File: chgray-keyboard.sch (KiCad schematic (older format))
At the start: 1 part, among them U1 Teensy2.0_(C)

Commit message: laying out the keys with logan
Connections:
- wire segments 69 -> 72
- no-connect marks 12 -> 11
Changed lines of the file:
@@
 $EndDescr
 $Sheet
-S 7300 1800 2100 1850
+S 7300 1800 2000 2800
 U 589645BF
 F0 "Keyboard Keys" 60
 F1 "Keys.sch" 60
 F2 "KEY_COL0" I L 7300 2000 60
-F3 "KEY_ROW0" I R 9400 1950 60
-F4 "KEY_ROW1" I R 9400 2150 60
+F3 "KEY_ROW0" I R 9300 1950 60
+F4 "KEY_ROW1" I R 9300 2150 60
 F5 "KEY_COL1" I L 7300 2150 60
-F6 "KEY_ROW2" I R 9400 2350 50
-F7 "KEY_ROW3" I R 9400 2550 50
-F8 "KEY_ROW4" I R 9400 2750 50
-F9 "KEY_ROW5" I R 9400 2900 50
+F6 "KEY_ROW2" I R 9300 2350 50
+F7 "KEY_ROW3" I R 9300 2550 50
+F8 "KEY_ROW4" I R 9300 2750 50
+F9 "KEY_ROW5" I R 9300 2900 50
 F10 "KEY_COL2" I L 7300 2300 50
 F11 "KEY_COL3" I L 7300 2450 50
@@
 F17 "KEY_COL9" I L 7300 3350 50
 F18 "KEY_COL10" I L 7300 3500 50
+F19 "KEY_COL11" I L 7300 3700 50
 $EndSheet
 Wire Wire Line
@@
 NoConn ~ 4550 6350
 NoConn ~ 4550 6450
-NoConn ~ 4550 6550
 NoConn ~ 2150 6250
 NoConn ~ 2150 6350
@@
 	2000 7150 2000 7650
 Connection ~ 2000 7150
+Wire Wire Line
+	7300 3700 4750 3700
+Wire Wire Line
+	4750 3700 4750 6550
+Wire Wire Line
+	4750 6550 4550 6550
 $EndSCHEMATC

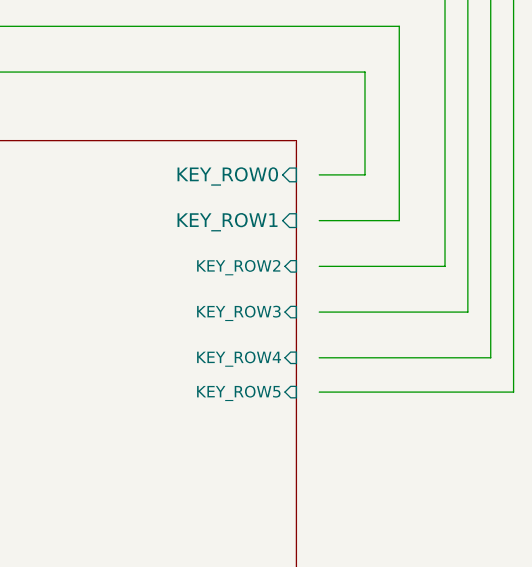
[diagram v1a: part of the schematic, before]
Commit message: add 1.75U switch
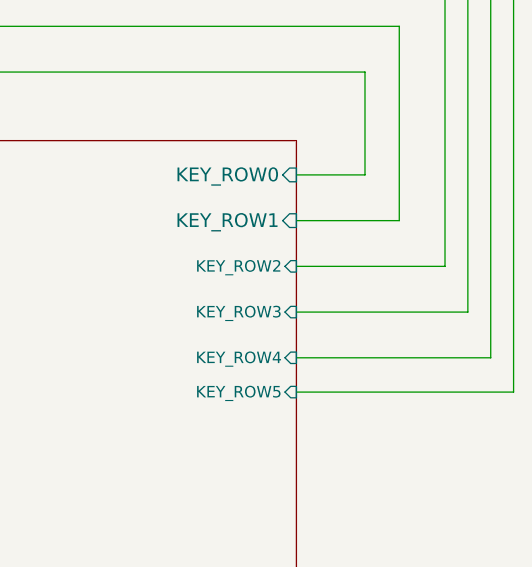
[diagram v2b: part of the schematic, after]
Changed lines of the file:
@@
 	7300 2000 1650 2000
 Wire Wire Line
-	9750 2150 9400 2150
-Wire Wire Line
-	9400 1950 9600 1950
-Wire Wire Line
 	1500 2150 7300 2150
-Wire Wire Line
-	9400 2350 9950 2350
 Wire Wire Line
 	9950 2350 9950 1000
 Wire Wire Line
 	9950 1000 1000 1000
-Wire Wire Line
-	9400 2550 10050 2550
 Wire Wire Line
 	10050 2550 10050 850
@@
 	10150 700  10150 2750
 Wire Wire Line
-	10150 2750 9400 2750
-Wire Wire Line
 	10250 2900 10250 550
 Wire Wire Line
 	10250 550  700  550
-Wire Wire Line
-	10250 2900 9400 2900
 Wire Wire Line
 	2250 5850 2150 5850
@@
 Wire Wire Line
 	4750 6550 4550 6550
+Wire Wire Line
+	9300 1950 9600 1950
+Wire Wire Line
+	9300 2150 9750 2150
+Wire Wire Line
+	9300 2350 9950 2350
+Wire Wire Line
+	9300 2550 10050 2550
+Wire Wire Line
+	9300 2750 10150 2750
+Wire Wire Line
+	9300 2900 10250 2900
 $EndSCHEMATC

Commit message: working on rgb
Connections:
- wire segments 72 -> 87
- no-connect marks 11 -> 7
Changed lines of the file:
@@
 $Descr A 11000 8500
 encoding utf-8
-Sheet 1 2
+Sheet 1 3
 Title ""
 Date ""
@@
 F18 "KEY_COL10" I L 7300 3500 50
 F19 "KEY_COL11" I L 7300 3700 50
+F20 "KEY_COL12" I L 7300 3950 50
+F21 "KEY_COL13" I L 7300 4150 50
 $EndSheet
 Wire Wire Line
@@
 Wire Wire Line
 	1500 2150 7300 2150
-Wire Wire Line
-	9950 2350 9950 1000
-Wire Wire Line
-	9950 1000 1000 1000
 Wire Wire Line
 	10050 2550 10050 850
@@
 	900  850  900  7250
 Wire Wire Line
-	1000 1000 1000 7050
-Wire Wire Line
 	1150 6950 2150 6950
 Wire Wire Line
@@
 NoConn ~ 4550 5950
 NoConn ~ 4550 6050
-NoConn ~ 4550 6150
-NoConn ~ 4550 6250
-NoConn ~ 4550 6350
-NoConn ~ 4550 6450
 NoConn ~ 2150 6250
 NoConn ~ 2150 6350
@@
 	9300 2150 9750 2150
 Wire Wire Line
-	9300 2350 9950 2350
-Wire Wire Line
 	9300 2550 10050 2550
 Wire Wire Line
@@
 Wire Wire Line
 	9300 2900 10250 2900
+$Sheet
+S 8250 5700 1600 600
+U 6096EA02
+F0 "Sheet6096EA01" 50
+F1 "RGB-Circuit.sch" 50
+F2 "LED_INPUT" I L 8250 5850 50
+F3 "LED_VDD" I L 8250 6150 50
+$EndSheet
+Wire Wire Line
+	8250 5850 6300 5850
+Wire Wire Line
+	6300 5850 6300 6450
+Wire Wire Line
+	6300 6450 4550 6450
+Wire Wire Line
+	8250 6150 6400 6150
+Wire Wire Line
+	6400 6150 6400 7450
+Wire Wire Line
+	6400 7450 1650 7450
+Wire Wire Line
+	1650 7450 1650 7050
+Wire Wire Line
+	1650 7050 2150 7050
+Wire Wire Line
+	9300 2350 9450 2350
+Wire Wire Line
+	9450 2350 9450 5550
+Wire Wire Line
+	9450 5550 4900 5550
+Wire Wire Line
+	4900 5550 4900 6150
+Wire Wire Line
+	4900 6150 4550 6150
+Wire Wire Line
+	4550 6250 6800 6250
+Wire Wire Line
+	6800 6250 6800 3950
+Wire Wire Line
+	6800 3950 7300 3950
+Wire Wire Line
+	7300 4150 7000 4150
+Wire Wire Line
+	7000 4150 7000 6350
+Wire Wire Line
+	7000 6350 4550 6350
 $EndSCHEMATC

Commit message: rgb
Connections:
- wire segments 87 -> 90
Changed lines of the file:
@@
 	2000 7150 2150 7150
 $Comp
-L power:GND #PWR0101
+L power:GND #PWR01
 U 1 1 6093A5EC
 P 2000 7650
-F 0 "#PWR0101" H 2000 7400 50  0001 C CNN
+F 0 "#PWR01" H 2000 7400 50  0001 C CNN
 F 1 "GND" H 2005 7477 50  0000 C CNN
 F 2 "" H 2000 7650 50  0001 C CNN
@@
 Wire Wire Line
 	9300 2900 10250 2900
-$Sheet
-S 8250 5700 1600 600
-U 6096EA02
-F0 "Sheet6096EA01" 50
-F1 "RGB-Circuit.sch" 50
-F2 "LED_INPUT" I L 8250 5850 50
-F3 "LED_VDD" I L 8250 6150 50
-$EndSheet
 Wire Wire Line
 	8250 5850 6300 5850
@@
 Wire Wire Line
 	7000 6350 4550 6350
+$Sheet
+S 8250 5700 1600 600
+U 6096EA02
+F0 "Sheet6096EA01" 50
+F1 "RGB-Circuit.sch" 50
+F2 "5V" I L 8250 6150 50
+F3 "VDD" I L 8250 6000 50
+F4 "INPUT" I L 8250 5850 50
+$EndSheet
+$Comp
+L power:GND #PWR02
+U 1 1 60D5C704
+P 7950 6550
+F 0 "#PWR02" H 7950 6300 50  0001 C CNN
+F 1 "GND" H 7955 6377 50  0000 C CNN
+F 2 "" H 7950 6550 50  0001 C CNN
+F 3 "" H 7950 6550 50  0001 C CNN
+	1    7950 6550
+	1    0    0    -1
+$EndComp
+Wire Wire Line
+	7950 6550 7900 6550
+Wire Wire Line
+	7900 6550 7900 6000
+Wire Wire Line
+	7900 6000 8250 6000
 $EndSCHEMATC

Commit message: keyboard
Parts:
- added J1: Conn_01x01_Female, Connector_PinHeader_1.27mm:PinHeader_2x07_P1.27mm_Vertical, symbol Connector_Generic:Conn_02x07_Odd_Even
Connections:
- wire segments 90 -> 108
- no-connect marks 7 -> 11
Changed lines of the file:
@@
 Wire Wire Line
 	1500 2150 1500 6750
-Wire Wire Line
-	1650 6650 2150 6650
-Wire Wire Line
-	1650 2000 1650 6650
 NoConn ~ 4550 5850
 NoConn ~ 4550 5950
-NoConn ~ 4550 6050
 NoConn ~ 2150 6250
 NoConn ~ 2150 6350
-NoConn ~ 2150 6450
-NoConn ~ 2150 6550
 Wire Wire Line
 	2150 5950 800  5950
@@
 $EndComp
 Wire Wire Line
-	2000 7150 2000 7650
+	2000 7150 2000 7600
 Connection ~ 2000 7150
 Wire Wire Line
@@
 	9300 2900 10250 2900
 Wire Wire Line
-	8250 5850 6300 5850
-Wire Wire Line
-	6300 5850 6300 6450
-Wire Wire Line
-	6300 6450 4550 6450
-Wire Wire Line
-	8250 6150 6400 6150
-Wire Wire Line
-	6400 6150 6400 7450
-Wire Wire Line
-	6400 7450 1650 7450
-Wire Wire Line
-	1650 7450 1650 7050
-Wire Wire Line
-	1650 7050 2150 7050
-Wire Wire Line
 	9300 2350 9450 2350
 Wire Wire Line
@@
 Wire Wire Line
 	4550 6250 6800 6250
-Wire Wire Line
-	6800 6250 6800 3950
 Wire Wire Line
 	6800 3950 7300 3950
@@
 $EndSheet
 $Comp
-L power:GND #PWR02
-U 1 1 60D5C704
-P 7950 6550
-F 0 "#PWR02" H 7950 6300 50  0001 C CNN
-F 1 "GND" H 7955 6377 50  0000 C CNN
-F 2 "" H 7950 6550 50  0001 C CNN
-F 3 "" H 7950 6550 50  0001 C CNN
-	1    7950 6550
+L Connector_Generic:Conn_02x07_Odd_Even J1
+U 1 1 609EE309
+P 7300 6900
+F 0 "J1" H 7350 7417 50  0000 C CNN
+F 1 "Conn_01x01_Female" H 7350 7326 50  0000 C CNN
+F 2 "Connector_PinHeader_1.27mm:PinHeader_2x07_P1.27mm_Vertical" H 7300 6900 50  0001 C CNN
+F 3 "~" H 7300 6900 50  0001 C CNN
+	1    7300 6900
 	1    0    0    -1
 $EndComp
 Wire Wire Line
-	7950 6550 7900 6550
+	7100 6600 6600 6600
 Wire Wire Line
-	7900 6550 7900 6000
+	6600 6600 6600 7600
 Wire Wire Line
-	7900 6000 8250 6000
+	6600 7600 2000 7600
+Connection ~ 2000 7600
+Wire Wire Line
+	2000 7600 2000 7650
+Wire Wire Line
+	6800 6250 6800 3950
+Wire Wire Line
+	6700 6050 6700 7200
+Wire Wire Line
+	6700 7200 7100 7200
+Wire Wire Line
+	7600 7200 8100 7200
+Wire Wire Line
+	8100 7200 8100 6150
+Wire Wire Line
+	8100 6150 8250 6150
+Wire Wire Line
+	7600 6600 7950 6600
+Wire Wire Line
+	7950 6600 7950 6000
+Wire Wire Line
+	7950 6000 8250 6000
+Wire Wire Line
+	7600 6700 8050 6700
+Wire Wire Line
+	8050 6700 8050 5850
+Wire Wire Line
+	8050 5850 8250 5850
+Wire Wire Line
+	4550 6450 7000 6450
+Wire Wire Line
+	7000 6450 7000 6700
+Wire Wire Line
+	7000 6700 7100 6700
+Wire Wire Line
+	4550 6050 6700 6050
+Wire Wire Line
+	2150 6450 1650 6450
+Wire Wire Line
+	1650 6450 1650 2000
+Wire Wire Line
+	7100 6800 6500 6800
+Wire Wire Line
+	6500 6800 6500 7950
+Wire Wire Line
+	6500 7950 1750 7950
+Wire Wire Line
+	1750 7950 1750 6550
+Wire Wire Line
+	1750 6550 2150 6550
+Wire Wire Line
+	2150 6650 1850 6650
+Wire Wire Line
+	1850 6650 1850 7850
+Wire Wire Line
+	1850 7850 6650 7850
+Wire Wire Line
+	6650 7850 6650 6900
+Wire Wire Line
+	6650 6900 7100 6900
+NoConn ~ 2150 7050
+NoConn ~ 7100 7000
+NoConn ~ 7100 7100
+NoConn ~ 7600 7000
+NoConn ~ 7600 7100
+NoConn ~ 7600 6900
+NoConn ~ 7600 6800
 $EndSCHEMATC

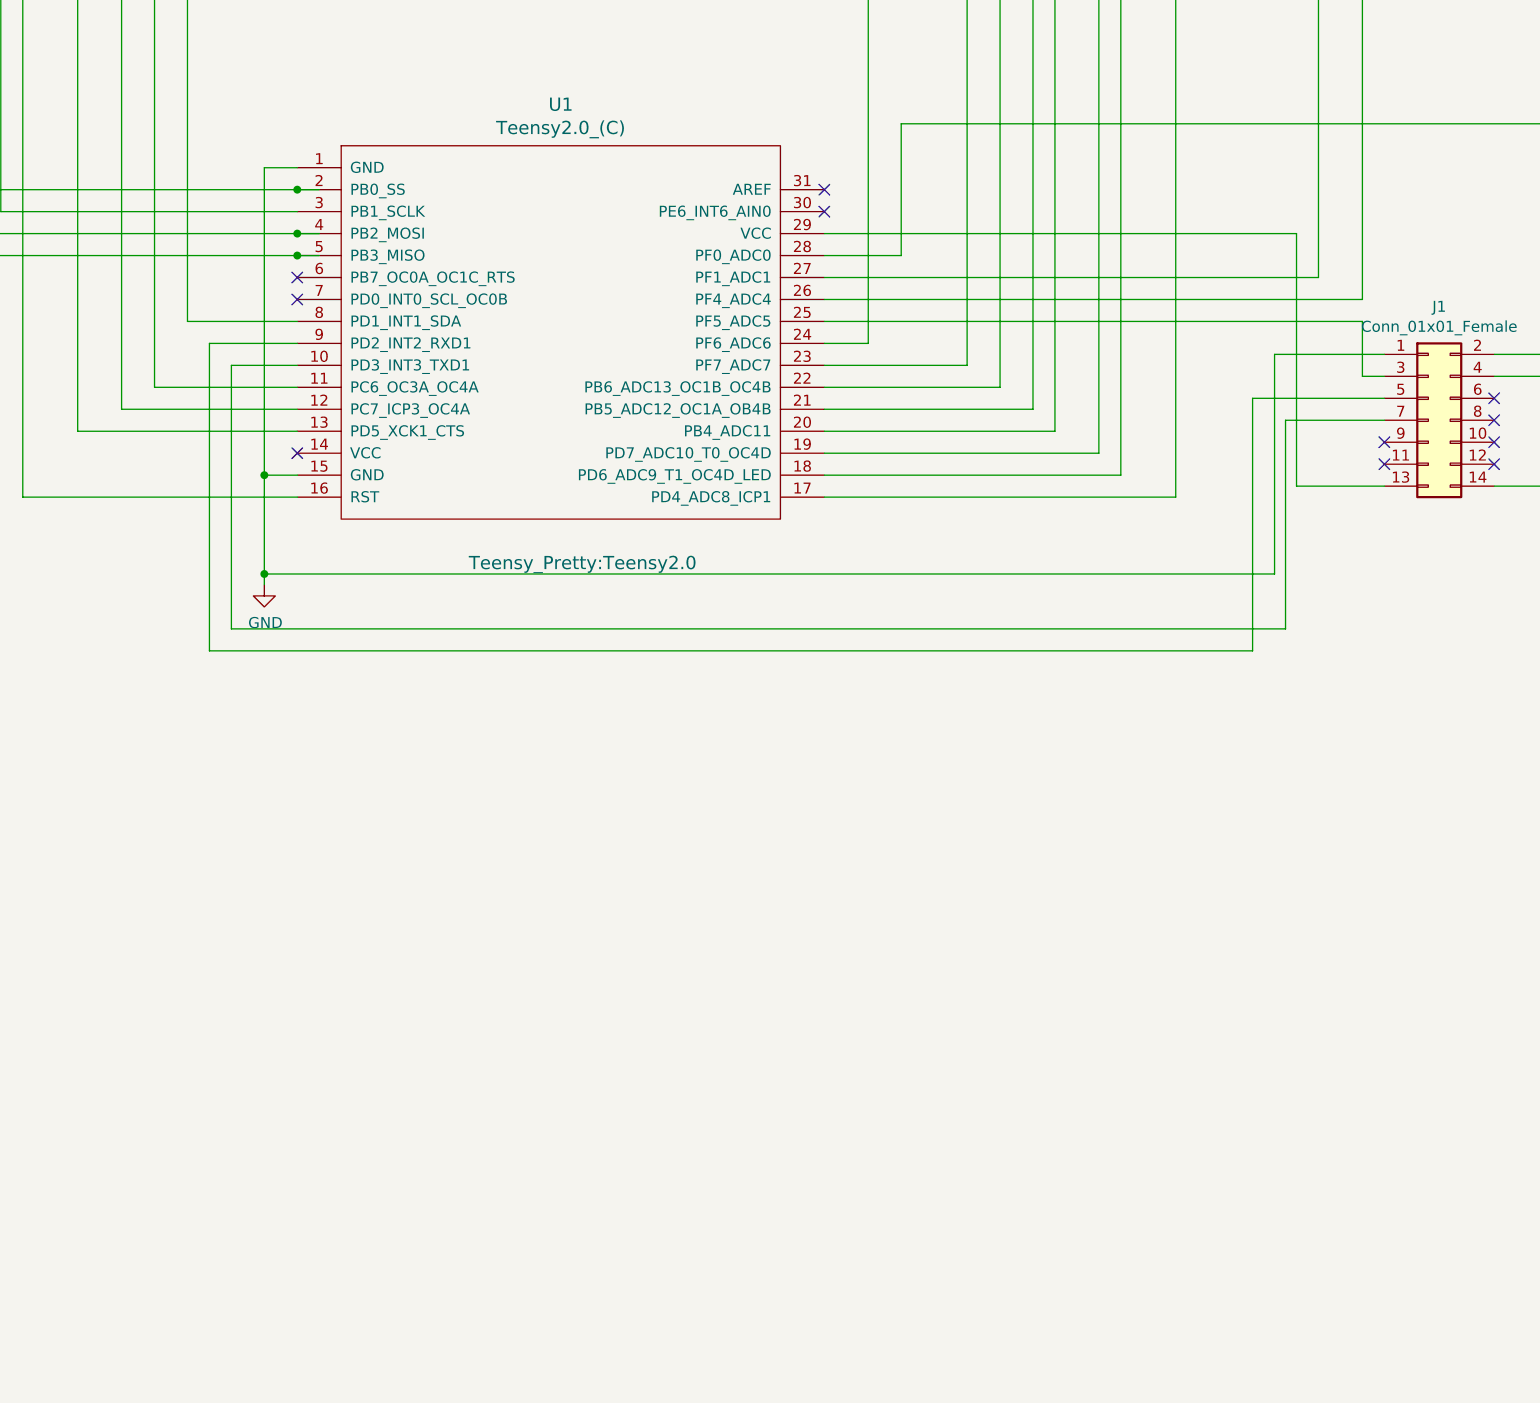
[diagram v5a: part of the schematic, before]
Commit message: Logan signed off on board location
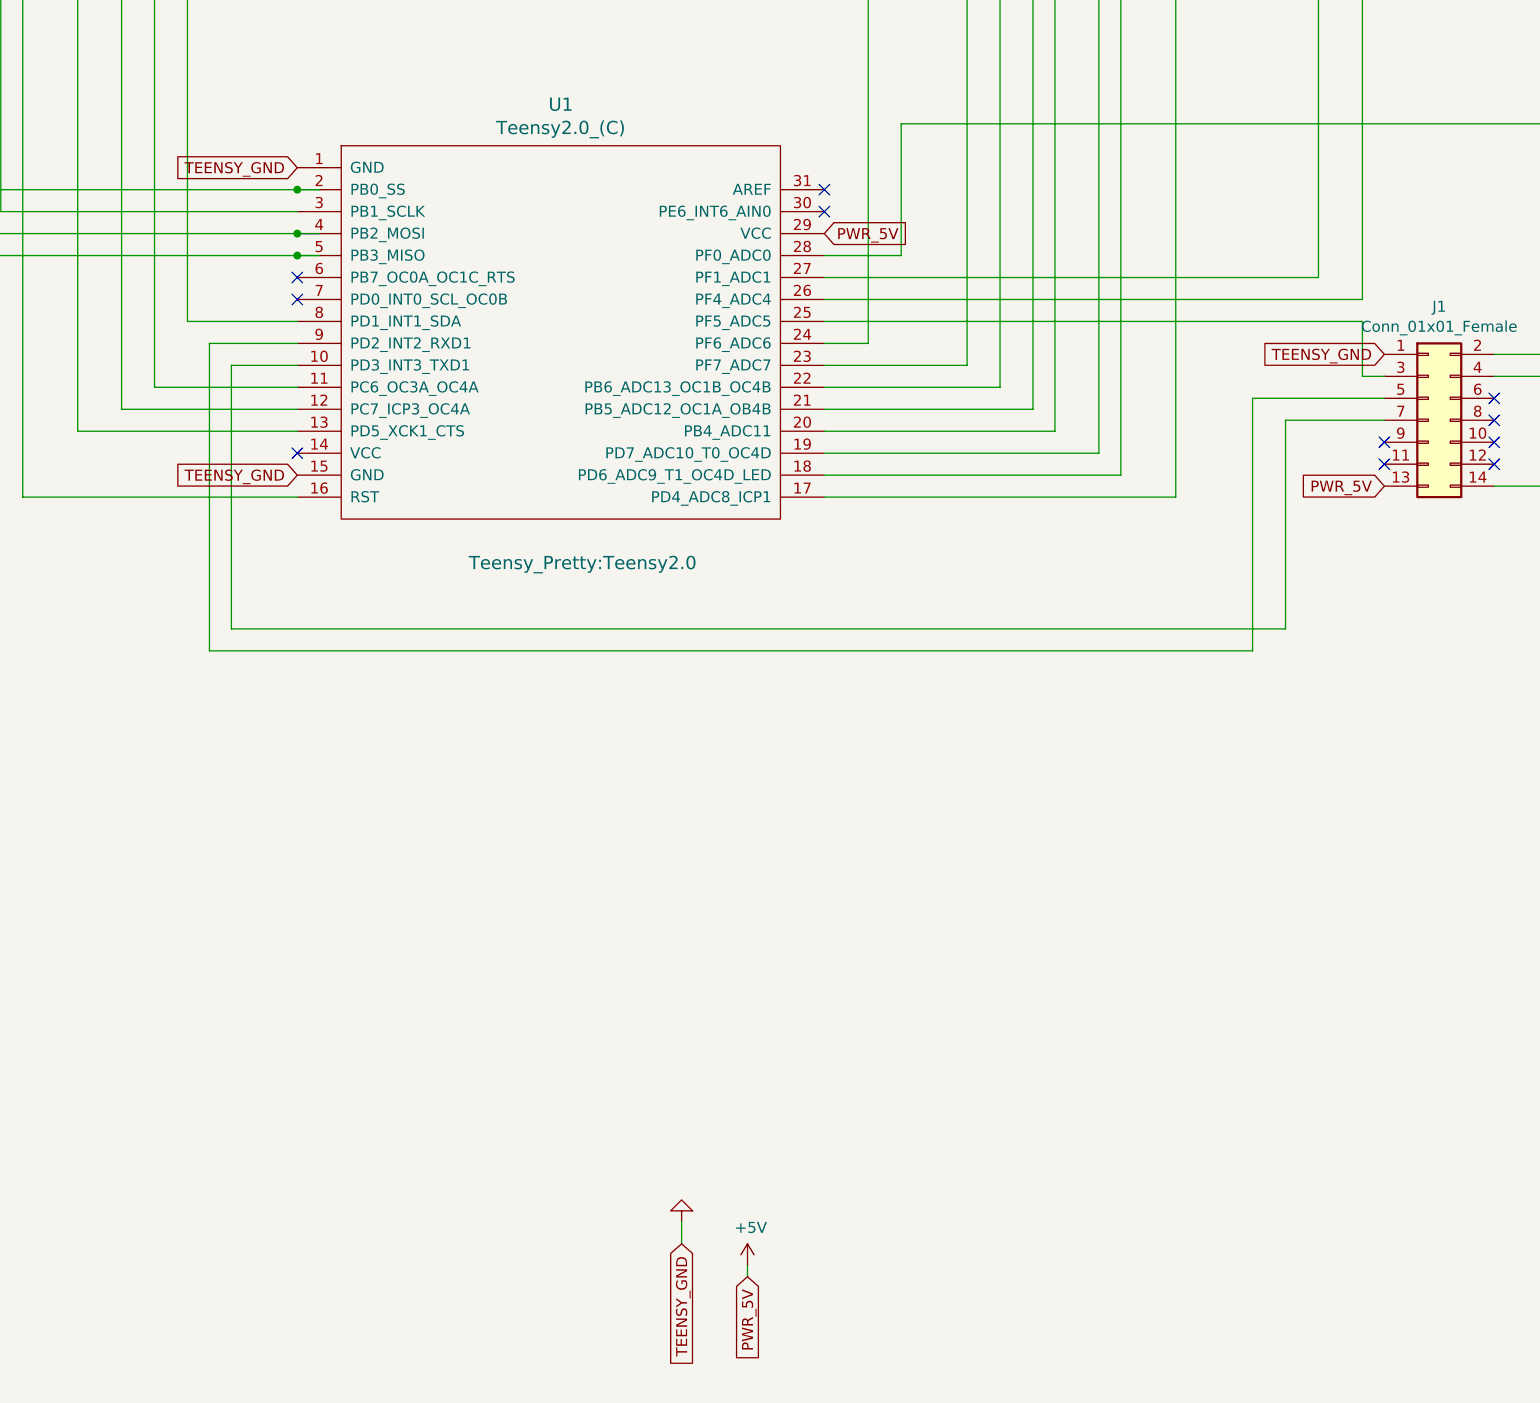
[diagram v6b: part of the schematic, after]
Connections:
- net labels added: +5V, PWR_5V, TEENSY_GND
- wire segments 108 -> 99
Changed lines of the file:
@@
 	800  5950 800  700
-Wire Wire Line
-	2150 5750 2000 5750
-Wire Wire Line
-	2000 5750 2000 7150
-Wire Wire Line
-	2000 7150 2150 7150
-$Comp
-L power:GND #PWR01
-U 1 1 6093A5EC
-P 2000 7650
-F 0 "#PWR01" H 2000 7400 50  0001 C CNN
-F 1 "GND" H 2005 7477 50  0000 C CNN
-F 2 "" H 2000 7650 50  0001 C CNN
-F 3 "" H 2000 7650 50  0001 C CNN
-	1    2000 7650
-	1    0    0    -1
-$EndComp
-Wire Wire Line
-	2000 7150 2000 7600
-Connection ~ 2000 7150
 Wire Wire Line
 	7300 3700 4750 3700
@@
 $EndComp
 Wire Wire Line
-	7100 6600 6600 6600
-Wire Wire Line
-	6600 6600 6600 7600
-Wire Wire Line
-	6600 7600 2000 7600
-Connection ~ 2000 7600
-Wire Wire Line
-	2000 7600 2000 7650
-Wire Wire Line
 	6800 6250 6800 3950
-Wire Wire Line
-	6700 6050 6700 7200
-Wire Wire Line
-	6700 7200 7100 7200
-Wire Wire Line
-	7600 7200 8100 7200
 Wire Wire Line
 	8100 7200 8100 6150
 Wire Wire Line
 	8100 6150 8250 6150
-Wire Wire Line
-	7600 6600 7950 6600
 Wire Wire Line
 	7950 6600 7950 6000
@@
 Wire Wire Line
 	7000 6700 7100 6700
-Wire Wire Line
-	4550 6050 6700 6050
 Wire Wire Line
 	2150 6450 1650 6450
@@
 NoConn ~ 7600 6900
 NoConn ~ 7600 6800
+Wire Wire Line
+	7600 7200 8100 7200
+$Comp
+L power:+5V #PWR0101
+U 1 1 6123E4B4
+P 4200 10750
+F 0 "#PWR0101" H 4200 10600 50  0001 C CNN
+F 1 "+5V" H 4215 10923 50  0000 C CNN
+F 2 "" H 4200 10750 50  0001 C CNN
+F 3 "" H 4200 10750 50  0001 C CNN
+	1    4200 10750
+	1    0    0    -1
+$EndComp
+Text GLabel 7100 7200 0    50   Input ~ 0
+PWR_5V
+Text GLabel 4200 10800 3    50   Input ~ 0
+PWR_5V
+Text GLabel 4550 6050 2    50   Input ~ 0
+PWR_5V
+Text GLabel 3900 10650 3    50   Input ~ 0
+TEENSY_GND
+Text GLabel 7100 6600 0    50   Input ~ 0
+TEENSY_GND
+Text GLabel 2150 5750 0    50   Input ~ 0
+TEENSY_GND
+Text GLabel 2150 7150 0    50   Input ~ 0
+TEENSY_GND
+$Comp
+L Cherry-Symbol:GND #PWR0102
+U 1 1 61266E57
+P 3900 10500
+F 0 "#PWR0102" H 3900 10500 30  0001 C CNN
+F 1 "GND" H 3900 10430 30  0001 C CNN
+F 2 "" H 3900 10500 50  0001 C CNN
+F 3 "" H 3900 10500 50  0001 C CNN
+	1    3900 10500
+	-1   0    0    1
+$EndComp
+Wire Wire Line
+	7600 6600 7950 6600
+Wire Wire Line
+	4200 10800 4200 10750
+Wire Wire Line
+	3900 10650 3900 10550
 $EndSCHEMATC
